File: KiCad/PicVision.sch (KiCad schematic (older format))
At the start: 38 parts, among them CON1 Power input, J1 video out, J2 audio_out, P1 ICSP, P2 I2C 1, P3 I2C 2, P4 gamepad 1, P5 gamepad 2, P6 spare I/O, SW1 SPST, SW2 reset, U1 UA78M33, U2 PIC24FJ64GA002, X1 8Mhz

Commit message: Began software work.
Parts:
- removed P6: spare I/O, symbol CONN_6
- added D3: 1N4148, symbol DIODE
- added P6: spare i/o, symbol CONN_4
- added R9: 1K2, ~, symbol R
- D2: value DIODE -> 1N4148
- renumbered R9 to R10, R10 to R11, R11 to R12
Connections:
- wire segments 121 -> 119
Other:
- note added: "NOTES:\nPIN 14 OC2 video sync\nPIN 15 SDO1 video data\nPIN 16 OC1 audio PWM\nPIN 21 OC3 video out pedestal\nPIN 22 SSC1 SP1 sync input"
- note removed: "NOTES:\nPIN 14 OC2 video sync\nPIN 15 SDO1 video data\nPIN 16 OC1 audio PWM\n"
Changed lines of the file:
@@
 LIBS:contrib
 LIBS:valves
-LIBS:librairie-personnelle
+LIBS:PicVision-cache
 EELAYER 27 0
 EELAYER END
@@
 Sheet 1 1
 Title ""
-Date "25 feb 2014"
+Date "27 feb 2014"
 Rev ""
 Comp ""
@@
 $EndComp
 $Comp
-L R R10
+L R R11
 U 1 1 530CC92A
 P 7350 4700
-F 0 "R10" V 7430 4700 50  0000 C CNN
+F 0 "R11" V 7430 4700 50  0000 C CNN
 F 1 "75R" V 7350 4700 50  0000 C CNN
 F 2 "" H 7350 4700 60  0000 C CNN
@@
 $EndComp
 $Comp
-L R R11
+L R R12
 U 1 1 530CC937
 P 7350 4950
-F 0 "R11" V 7430 4950 50  0000 C CNN
+F 0 "R12" V 7430 4950 50  0000 C CNN
 F 1 "470R" V 7350 4950 50  0000 C CNN
 F 2 "" H 7350 4950 60  0000 C CNN
@@
 P 6800 4700
 F 0 "D2" H 6800 4800 40  0000 C CNN
-F 1 "DIODE" H 6800 4600 40  0000 C CNN
+F 1 "1N4148" H 6800 4600 40  0000 C CNN
 F 2 "" H 6800 4700 60  0000 C CNN
 F 3 "" H 6800 4700 60  0000 C CNN
@@
 $EndComp
 $Comp
-L R R9
+L R R10
 U 1 1 530CD0AB
 P 7100 5650
-F 0 "R9" V 7180 5650 50  0000 C CNN
+F 0 "R10" V 7180 5650 50  0000 C CNN
 F 1 "200R" V 7100 5650 50  0000 C CNN
 F 2 "" H 7100 5650 60  0000 C CNN
@@
 SDA2
 Text Notes 9350 5050 0    59   ~ 0
-NOTES:\nPIN 14 OC2    video sync\nPIN 15 SDO1  video data\nPIN 16 OC1    audio PWM\n
+NOTES:\nPIN 14 OC2    video sync\nPIN 15 SDO1  video data\nPIN 16 OC1    audio PWM\nPIN 21 OC3    video out pedestal\nPIN 22 SSC1  SP1 sync input
 Text GLabel 6300 4100 2    39   Input ~ 0
 SCL1
@@
 CS1
 $Comp
-L CONN_6 P6
-U 1 1 530CF1D0
-P 8450 3400
-F 0 "P6" V 8400 3400 60  0000 C CNN
-F 1 "spare I/O" V 8500 3400 60  0000 C CNN
-F 2 "" H 8450 3400 60  0000 C CNN
-F 3 "" H 8450 3400 60  0000 C CNN
-	1    8450 3400
-	1    0    0    -1
-$EndComp
-$Comp
 L GND #PWR18
 U 1 1 530CF1DF
@@
 	1    0    0    -1
 $EndComp
-Text GLabel 8100 3050 1    60   Input ~ 0
+Text GLabel 8100 3250 1    60   Input ~ 0
 Vdd
 $Comp
@@
 	2700 2350 2700 2400
 Wire Wire Line
-	7600 4700 7600 4950
+	7600 3650 7600 4950
 Wire Wire Line
 	7600 4700 7700 4700
@@
 	8100 3650 8100 3800
 Wire Wire Line
-	8100 3050 8100 3150
-Wire Wire Line
-	6250 3700 7900 3700
-Wire Wire Line
-	7900 3700 7900 3550
-Wire Wire Line
-	7900 3550 8100 3550
-Wire Wire Line
-	6250 3600 7800 3600
-Wire Wire Line
-	7800 3600 7800 3450
+	8100 3250 8100 3350
+Wire Wire Line
+	7700 3550 8100 3550
 Wire Wire Line
 	7800 3450 8100 3450
@@
 	6250 3500 7700 3500
 Wire Wire Line
-	7700 3500 7700 3350
-Wire Wire Line
-	7700 3350 8100 3350
-Wire Wire Line
-	6250 3400 7600 3400
-Wire Wire Line
-	7600 3400 7600 3250
-Wire Wire Line
-	7600 3250 8100 3250
+	6250 3400 7800 3400
 Wire Wire Line
 	2300 6300 2300 6550
@@
 Wire Wire Line
 	5250 5650 6050 5650
+Wire Wire Line
+	6250 3600 6250 3700
+$Comp
+L R R9
+U 1 1 530EB8E3
+P 6550 3650
+F 0 "R9" V 6630 3650 40  0000 C CNN
+F 1 "1K2" V 6557 3651 40  0000 C CNN
+F 2 "~" V 6480 3650 30  0000 C CNN
+F 3 "~" H 6550 3650 30  0000 C CNN
+	1    6550 3650
+	0    -1   -1   0
+$EndComp
+$Comp
+L DIODE D3
+U 1 1 530EB8F0
+P 7100 3650
+F 0 "D3" H 7100 3750 40  0000 C CNN
+F 1 "1N4148" H 7100 3550 40  0000 C CNN
+F 2 "" H 7100 3650 60  0000 C CNN
+F 3 "" H 7100 3650 60  0000 C CNN
+	1    7100 3650
+	1    0    0    -1
+$EndComp
+Wire Wire Line
+	6300 3650 6250 3650
+Connection ~ 6250 3650
+Wire Wire Line
+	6800 3650 6900 3650
+Wire Wire Line
+	7300 3650 7600 3650
+Connection ~ 7600 4700
+$Comp
+L CONN_4 P6
+U 1 1 530EBBB0
+P 8450 3500
+F 0 "P6" V 8400 3500 50  0000 C CNN
+F 1 "spare i/o" V 8500 3500 50  0000 C CNN
+F 2 "" H 8450 3500 60  0000 C CNN
+F 3 "" H 8450 3500 60  0000 C CNN
+	1    8450 3500
+	1    0    0    -1
+$EndComp
+Wire Wire Line
+	7800 3400 7800 3450
+Wire Wire Line
+	7700 3500 7700 3550
 $EndSCHEMATC

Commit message: work on TVout
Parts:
- removed D3: 1N4148, symbol DIODE
- removed P6: spare i/o, symbol CONN_4
- removed R9: 1K2, ~, symbol R
- added F1: 500mA, ~, symbol FUSE
- added P4: PAL VIDEO, symbol CONN_2
- added R12: 10K, ~, symbol R
- renumbered P4 to P5, P5 to P6, R11 to R10, R12 to R11, R6 to R5, R5 to R6, R10 to R9
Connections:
- wire segments 119 -> 112
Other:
- note added: "short for PAL"
- moved on the sheet: CON1, D1, R6, SW1, U1

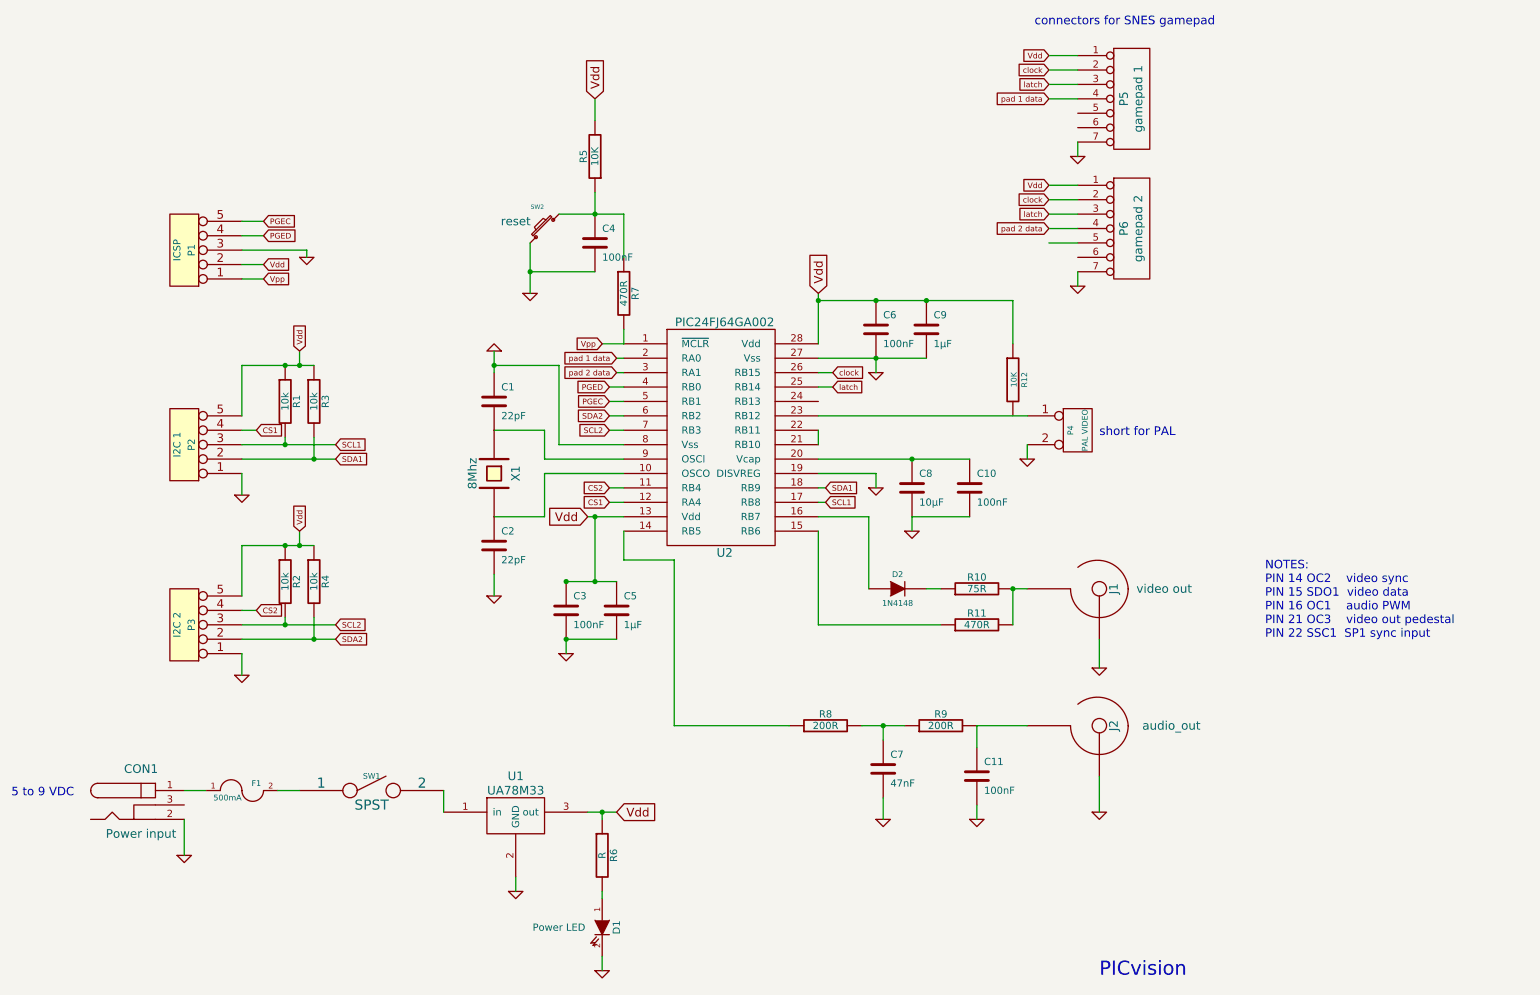
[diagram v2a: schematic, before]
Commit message: modification du schematic to account for switch PIC24FJ64GA002 by PIC32MX150F128B.
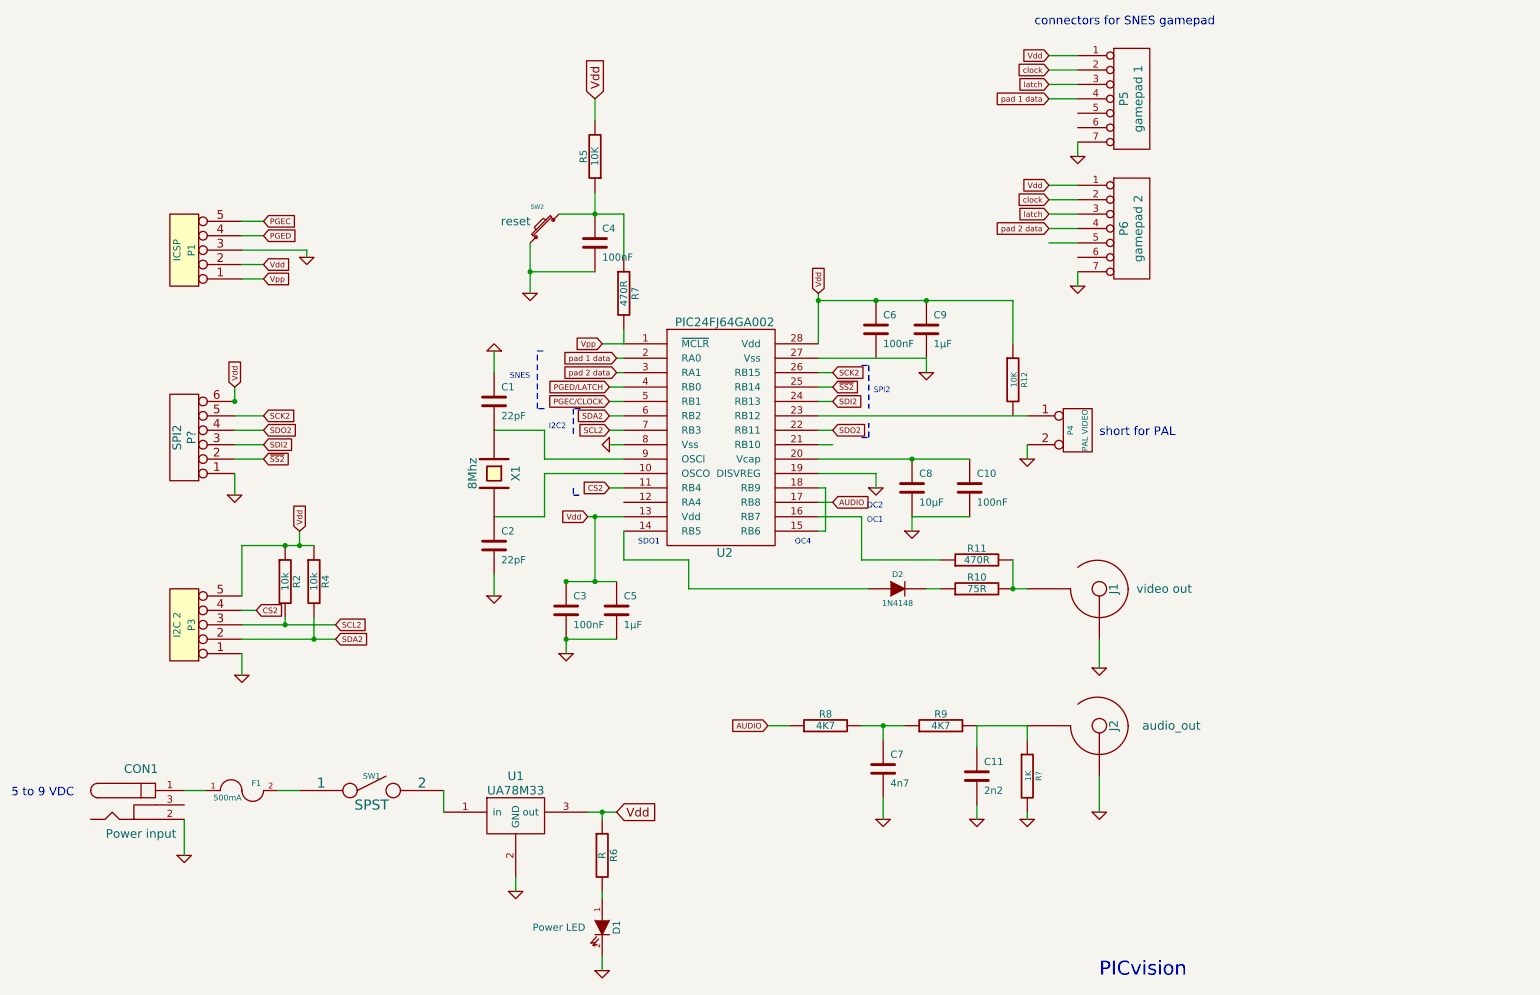
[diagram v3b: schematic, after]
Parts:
- removed P2: I2C 1, symbol CONN_5
- removed R1, R3: 10k, symbol R
- added P?: SPI2, symbol CONN_6
- added R?: 1K, ~, symbol R
- C11: value 100nF -> 2n2
- C7: value 47nF -> 4n7
- R8, R9: value 200R -> 4K7
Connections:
- net SDA1 is gone; now on an unnamed net: U2.18 (RB9)
- net GND: now also P?.1, R?.2; no longer C6.2
- net PGEC: no longer U2.5 (RB1)
- net PGED: no longer U2.4 (RB0)
- net Vdd: now also P?.6
- net clock: no longer U2.26 (RB15)
- net latch: no longer U2.25 (RB14)
- net at U2.14 (RB5): now also D2.1 (A); no longer R8.1
- net at U2.15 (RB6): no longer R11.1
- net at U2.16 (RB7): now also R11.1; no longer D2.1 (A)
- net at U2.21 (RB10): no longer U2.22 (RB11)
- net SDI2: now reaches U2.24 (RB13)
- net SDI2: now also P?.3
- net at C11.1, J2.~, R9.2: now also R?.1
- net CS1: no longer names the net of U2.12 (RA4)
- net SCL1 renamed AUDIO
- net AUDIO: now also R8.1
- new net PGEC/CLOCK: U2.5 (RB1)
- new net PGED/LATCH: U2.4 (RB0)
- new net SCK2: P?.5, U2.26 (RB15)
- new net SDO2: P?.4, U2.22 (RB11)
- new net ~SS2: P?.2, U2.25 (RB14)
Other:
- note added: "I2C2"
- note added: "OC1"
- note added: "OC2"
- note added: "OC4"
- note added: "SDO1"
- note added: "SNES"
- note added: "SPI2"
- note removed: "NOTES:\nPIN 14 OC2 video sync\nPIN 15 SDO1 video data\nPIN 16 OC1 audio PWM\nPIN 21 OC3 video out pedestal\nPIN 22 SSC1 SP1 sync input"
- moved on the sheet: R11

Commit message: schematic update
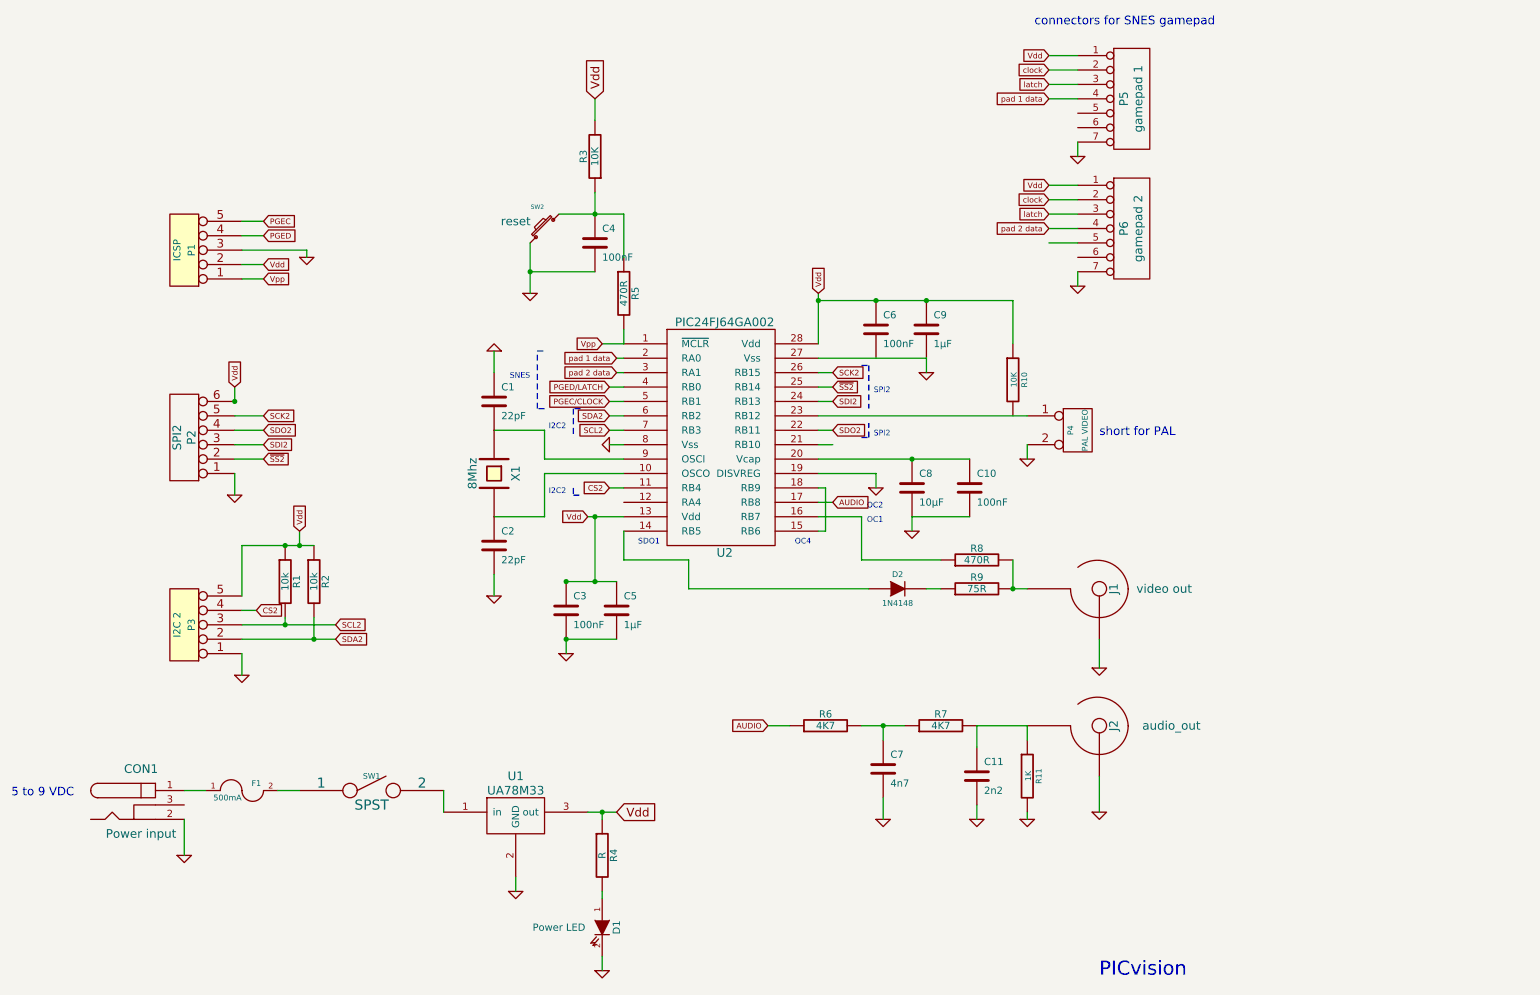
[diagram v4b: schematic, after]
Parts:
- gave numbers to parts that had none: 2
- renumbered R2 to R1, R12 to R10, R4 to R2, R5 to R3, R6 to R4, R7 to R5, R8 to R6, R9 to R7, R11 to R8, R10 to R9
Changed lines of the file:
@@
 $EndComp
 $Comp
-L GND #PWR11
+L GND #PWR15
 U 1 1 530CC30B
 P 7000 3200
-F 0 "#PWR11" H 7000 3200 30  0001 C CNN
+F 0 "#PWR15" H 7000 3200 30  0001 C CNN
 F 1 "GND" H 7000 3130 30  0001 C CNN
 F 2 "" H 7000 3200 60  0000 C CNN
@@
 $EndComp
 $Comp
-L R R5
+L R R3
 U 1 1 530CC59B
 P 4700 1700
-F 0 "R5" V 4780 1700 50  0000 C CNN
+F 0 "R3" V 4780 1700 50  0000 C CNN
 F 1 "10K" V 4700 1700 50  0000 C CNN
 F 2 "" H 4700 1700 60  0000 C CNN
@@
 $EndComp
 $Comp
-L R R7
+L R R5
 U 1 1 530CC6B2
 P 4900 2650
-F 0 "R7" V 4980 2650 50  0000 C CNN
+F 0 "R5" V 4980 2650 50  0000 C CNN
 F 1 "470R" V 4900 2650 50  0000 C CNN
 F 2 "" H 4900 2650 60  0000 C CNN
@@
 $EndComp
 $Comp
-L GND #PWR19
+L GND #PWR21
 U 1 1 530CC91B
 P 8200 5250
-F 0 "#PWR19" H 8200 5250 30  0001 C CNN
+F 0 "#PWR21" H 8200 5250 30  0001 C CNN
 F 1 "GND" H 8200 5180 30  0001 C CNN
 F 2 "" H 8200 5250 60  0000 C CNN
@@
 $EndComp
 $Comp
-L R R10
+L R R9
 U 1 1 530CC92A
 P 7350 4700
-F 0 "R10" V 7430 4700 50  0000 C CNN
+F 0 "R9" V 7430 4700 50  0000 C CNN
 F 1 "75R" V 7350 4700 50  0000 C CNN
 F 2 "" H 7350 4700 60  0000 C CNN
@@
 $EndComp
 $Comp
-L R R11
+L R R8
 U 1 1 530CC937
 P 7350 4500
-F 0 "R11" V 7430 4500 50  0000 C CNN
+F 0 "R8" V 7430 4500 50  0000 C CNN
 F 1 "470R" V 7350 4500 50  0000 C CNN
 F 2 "" H 7350 4500 60  0000 C CNN
@@
 $EndComp
 $Comp
-L GND #PWR18
+L GND #PWR20
 U 1 1 530CCADC
 P 8050 2600
-F 0 "#PWR18" H 8050 2600 30  0001 C CNN
+F 0 "#PWR20" H 8050 2600 30  0001 C CNN
 F 1 "GND" H 8050 2530 30  0001 C CNN
 F 2 "" H 8050 2600 60  0000 C CNN
@@
 $EndComp
 $Comp
-L GND #PWR17
+L GND #PWR19
 U 1 1 530CCAE9
 P 8050 1700
-F 0 "#PWR17" H 8050 1700 30  0001 C CNN
+F 0 "#PWR19" H 8050 1700 30  0001 C CNN
 F 1 "GND" H 8050 1630 30  0001 C CNN
 F 2 "" H 8050 1700 60  0000 C CNN
@@
 $EndComp
 $Comp
-L GND #PWR20
+L GND #PWR22
 U 1 1 530CD057
 P 8200 6250
-F 0 "#PWR20" H 8200 6250 30  0001 C CNN
+F 0 "#PWR22" H 8200 6250 30  0001 C CNN
 F 1 "GND" H 8200 6180 30  0001 C CNN
 F 2 "" H 8200 6250 60  0000 C CNN
@@
 $EndComp
 $Comp
-L R R9
+L R R7
 U 1 1 530CD0AB
 P 7100 5650
-F 0 "R9" V 7180 5650 50  0000 C CNN
+F 0 "R7" V 7180 5650 50  0000 C CNN
 F 1 "4K7" V 7100 5650 50  0000 C CNN
 F 2 "" H 7100 5650 60  0000 C CNN
@@
 $EndComp
 $Comp
-L GND #PWR15
+L GND #PWR16
 U 1 1 530CD0C7
 P 7350 6300
-F 0 "#PWR15" H 7350 6300 30  0001 C CNN
+F 0 "#PWR16" H 7350 6300 30  0001 C CNN
 F 1 "GND" H 7350 6230 30  0001 C CNN
 F 2 "" H 7350 6300 60  0000 C CNN
@@
 CS2
 $Comp
-L R R2
+L R R1
 U 1 1 530CD7B3
 P 2550 4650
-F 0 "R2" V 2630 4650 50  0000 C CNN
+F 0 "R1" V 2630 4650 50  0000 C CNN
 F 1 "10k" V 2550 4650 50  0000 C CNN
 F 2 "" H 2550 4650 60  0000 C CNN
@@
 $EndComp
 $Comp
-L R R4
+L R R2
 U 1 1 530CD7B9
 P 2750 4650
-F 0 "R4" V 2830 4650 50  0000 C CNN
+F 0 "R2" V 2830 4650 50  0000 C CNN
 F 1 "10k" V 2750 4650 50  0000 C CNN
 F 2 "" H 2750 4650 60  0000 C CNN
@@
 PICvision\n
 $Comp
-L R R6
+L R R4
 U 1 1 530CF92E
 P 4750 6550
-F 0 "R6" V 4830 6550 50  0000 C CNN
+F 0 "R4" V 4830 6550 50  0000 C CNN
 F 1 "R" V 4750 6550 50  0000 C CNN
 F 2 "" H 4750 6550 60  0000 C CNN
@@
 $EndComp
 $Comp
-L R R8
+L R R6
 U 1 1 530D024B
 P 6300 5650
-F 0 "R8" V 6380 5650 50  0000 C CNN
+F 0 "R6" V 6380 5650 50  0000 C CNN
 F 1 "4K7" V 6300 5650 50  0000 C CNN
 F 2 "" H 6300 5650 60  0000 C CNN
@@
 $EndComp
 $Comp
-L GND #PWR16
+L GND #PWR17
 U 1 1 530FB94C
 P 7700 3800
-F 0 "#PWR16" H 7700 3800 30  0001 C CNN
+F 0 "#PWR17" H 7700 3800 30  0001 C CNN
 F 1 "GND" H 7700 3730 30  0001 C CNN
 F 2 "" H 7700 3800 60  0000 C CNN
@@
 $EndComp
 $Comp
-L R R12
+L R R10
 U 1 1 530FEB9A
 P 7600 3250
-F 0 "R12" V 7680 3250 40  0000 C CNN
+F 0 "R10" V 7680 3250 40  0000 C CNN
 F 1 "10K" V 7607 3251 40  0000 C CNN
 F 2 "~" V 7530 3250 30  0000 C CNN
@@
 AUDIO
 $Comp
-L R R?
+L R R11
 U 1 1 53120662
 P 7700 6000
-F 0 "R?" V 7780 6000 40  0000 C CNN
+F 0 "R11" V 7780 6000 40  0000 C CNN
 F 1 "1K" V 7707 6001 40  0000 C CNN
 F 2 "~" V 7630 6000 30  0000 C CNN
@@
 $EndComp
 $Comp
-L GND #PWR?
+L GND #PWR18
 U 1 1 5312066F
 P 7700 6300
-F 0 "#PWR?" H 7700 6300 30  0001 C CNN
+F 0 "#PWR18" H 7700 6300 30  0001 C CNN
 F 1 "GND" H 7700 6230 30  0001 C CNN
 F 2 "" H 7700 6300 60  0000 C CNN
@@
 $EndComp
 $Comp
-L CONN_6 P?
+L CONN_6 P2
 U 1 1 53120789
 P 1850 3650
-F 0 "P?" V 1800 3650 60  0000 C CNN
+F 0 "P2" V 1800 3650 60  0000 C CNN
 F 1 "SPI2" V 1900 3650 60  0000 C CNN
 F 2 "" H 1850 3650 60  0000 C CNN
@@
 SNES
 $Comp
-L GND #PWR?
+L GND #PWR11
 U 1 1 53122248
 P 4800 3700
-F 0 "#PWR?" H 4800 3700 30  0001 C CNN
+F 0 "#PWR11" H 4800 3700 30  0001 C CNN
 F 1 "GND" H 4800 3630 30  0001 C CNN
 F 2 "" H 4800 3700 60  0000 C CNN
@@
 Text Notes 4500 3600 2    39   ~ 0
 I2C2
+Text Notes 4500 4050 2    39   ~ 0
+I2C2
+Text Notes 6750 3650 2    39   ~ 0
+SPI2
 $EndSCHEMATC

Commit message: work on sound.c
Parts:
- added R?: 10K, ~, symbol R
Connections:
- net NOISE: now reaches U2.21 (RB10)
- net NOISE: now also R?.1
- net at C11.1, J2.~, R11.1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: now also R?.2
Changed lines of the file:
@@
 Sheet 1 1
 Title ""
-Date "1 mar 2014"
+Date "3 mar 2014"
 Rev ""
 Comp ""
@@
 	7350 6200 7350 6300
 Wire Wire Line
-	7350 5650 7350 5800
+	7350 5300 7350 5800
 Wire Wire Line
 	7350 5650 7700 5650
@@
 Text Notes 6750 3650 2    39   ~ 0
 SPI2
+Text GLabel 6350 3700 2    39   Input ~ 0
+NOISE
+$Comp
+L R R?
+U 1 1 5314EEB5
+P 7050 5300
+F 0 "R?" V 7130 5300 40  0000 C CNN
+F 1 "10K" V 7057 5301 40  0000 C CNN
+F 2 "~" V 6980 5300 30  0000 C CNN
+F 3 "~" H 7050 5300 30  0000 C CNN
+	1    7050 5300
+	0    -1   -1   0
+$EndComp
+Text GLabel 6700 5300 0    39   Input ~ 0
+NOISE
+Wire Wire Line
+	6700 5300 6800 5300
+Wire Wire Line
+	7300 5300 7350 5300
+Connection ~ 7350 5650
 $EndSCHEMATC
